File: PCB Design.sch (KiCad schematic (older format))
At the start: 14 parts

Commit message: Main schematic finished
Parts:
- added D? (x4): D_Small, symbol Device:D_Small
- added F?: 500mA, symbol Device:Polyfuse_Small
- added MX? (x4): MX-NoLED, symbol MX_Alps_Hybrid:MX-NoLED
- added USB?: Molex-0548190589, symbol random-keyboard-parts:Molex-0548190589
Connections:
- net labels added: VCC, col0, col1, row0, row1
- wire segments 46 -> 72
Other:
- moved on the sheet: C?, R?, SW?, U?, Y?

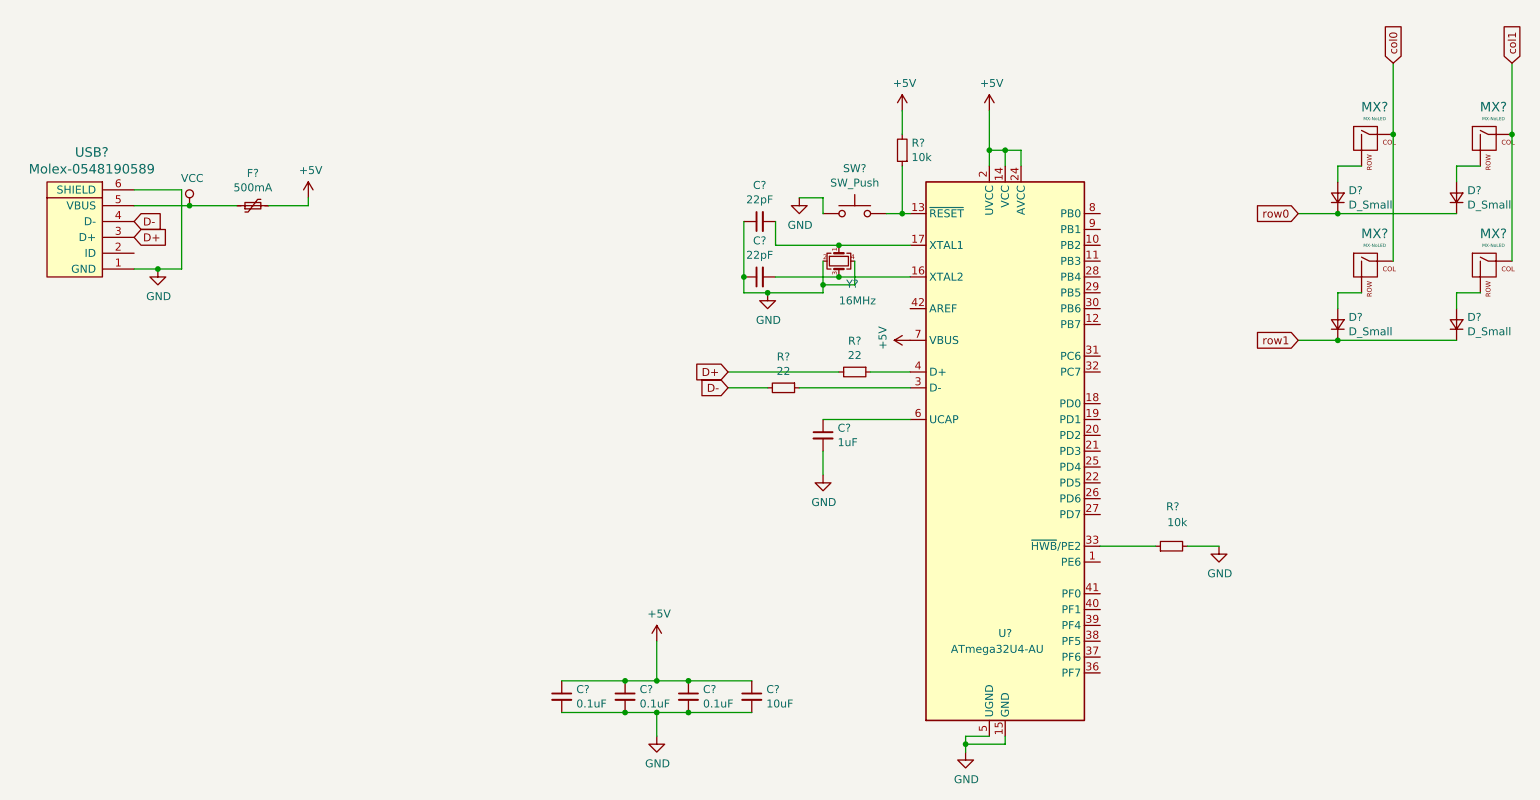
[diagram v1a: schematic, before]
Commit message: Assigning library components to schematic, need to figure out mx_alps_hybrid library issue
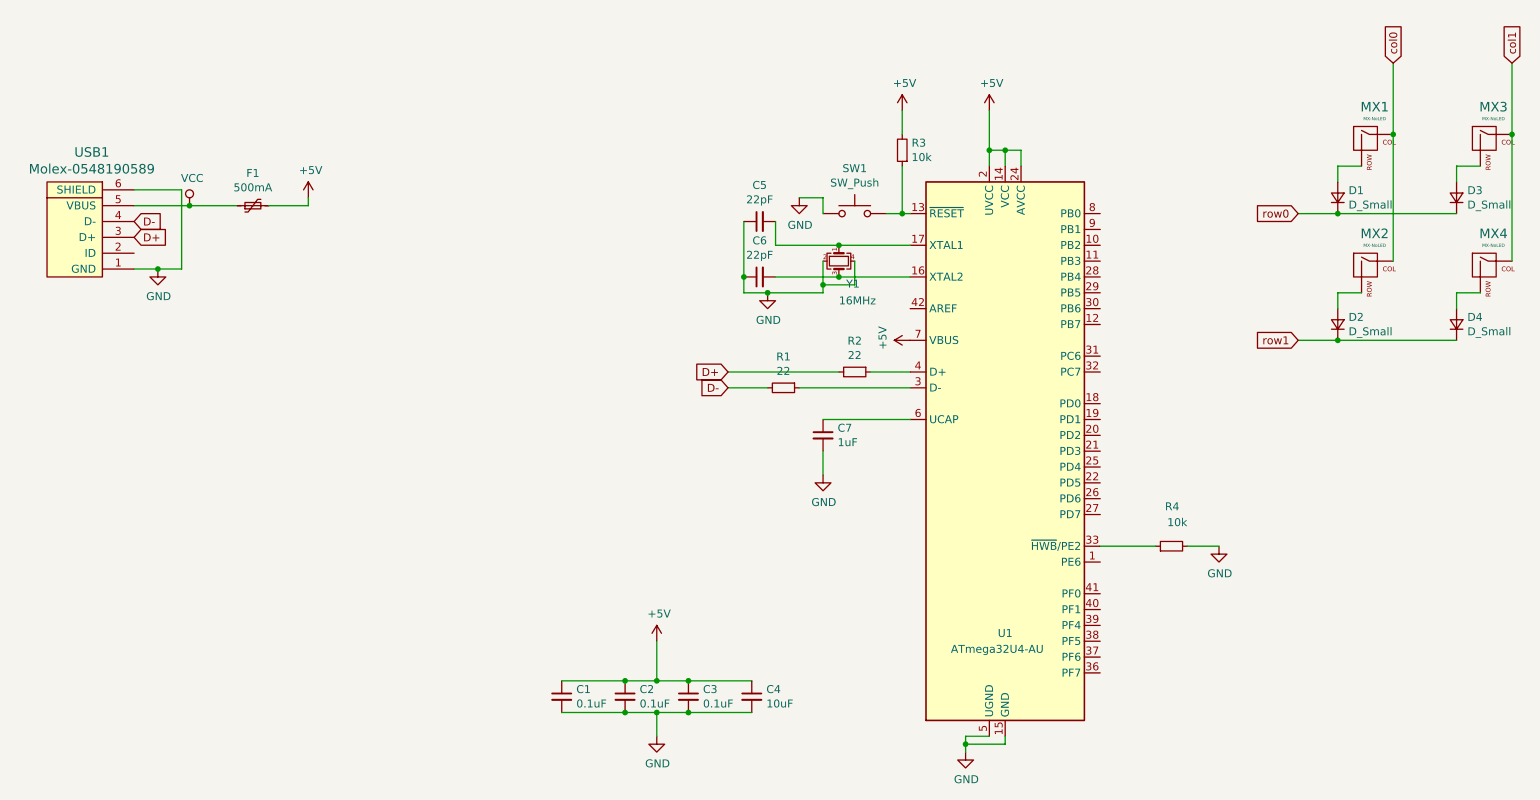
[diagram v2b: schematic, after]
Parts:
- C1, C2, C3, C4, C5, C6, C7: renamed from C?; footprint (none) -> Capacitor_SMD:C_0805_2012Metric
- D1, D2, D3, D4: renamed from D?; footprint (none) -> Diode_SMD:D_SOD-123
- F1: renamed from F?; footprint (none) -> Fuse:Fuse_1206_3216Metric
- R1, R2, R3, R4: renamed from R?; footprint (none) -> Resistor_SMD:R_0805_2012Metric
- SW1: renamed from SW?; footprint (none) -> random-keyboard-parts:SKQG-1155865
- USB1: renamed from USB?; footprint (none) -> random-keyboard-parts:Molex-0548190589
- Y1: renamed from Y?; footprint (none) -> Crystal:Crystal_SMD_3225-4Pin_3.2x2.5mm
- gave numbers to parts that had none: 5

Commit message: Figured out mx lib issue
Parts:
- MX1, MX2, MX3, MX4: footprint (none) -> MX_Alps_Hybrid1:MX-1U-NoLED
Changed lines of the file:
@@
 F 0 "MX1" H 10133 1523 60  0000 C CNN
 F 1 "MX-NoLED" H 10133 1449 20  0000 C CNN
-F 2 "" H 9475 1275 60  0001 C CNN
+F 2 "MX_Alps_Hybrid1:MX-1U-NoLED" H 9475 1275 60  0001 C CNN
 F 3 "" H 9475 1275 60  0001 C CNN
 	1    10100 1300
@@
 F 0 "MX3" H 10883 1523 60  0000 C CNN
 F 1 "MX-NoLED" H 10883 1449 20  0000 C CNN
-F 2 "" H 10225 1275 60  0001 C CNN
+F 2 "MX_Alps_Hybrid1:MX-1U-NoLED" H 10225 1275 60  0001 C CNN
 F 3 "" H 10225 1275 60  0001 C CNN
 	1    10850 1300
@@
 F 0 "MX2" H 10133 2323 60  0000 C CNN
 F 1 "MX-NoLED" H 10133 2249 20  0000 C CNN
-F 2 "" H 9475 2075 60  0001 C CNN
+F 2 "MX_Alps_Hybrid1:MX-1U-NoLED" H 9475 2075 60  0001 C CNN
 F 3 "" H 9475 2075 60  0001 C CNN
 	1    10100 2100
@@
 F 0 "MX4" H 10883 2323 60  0000 C CNN
 F 1 "MX-NoLED" H 10883 2249 20  0000 C CNN
-F 2 "" H 10225 2075 60  0001 C CNN
+F 2 "MX_Alps_Hybrid1:MX-1U-NoLED" H 10225 2075 60  0001 C CNN
 F 3 "" H 10225 2075 60  0001 C CNN
 	1    10850 2100

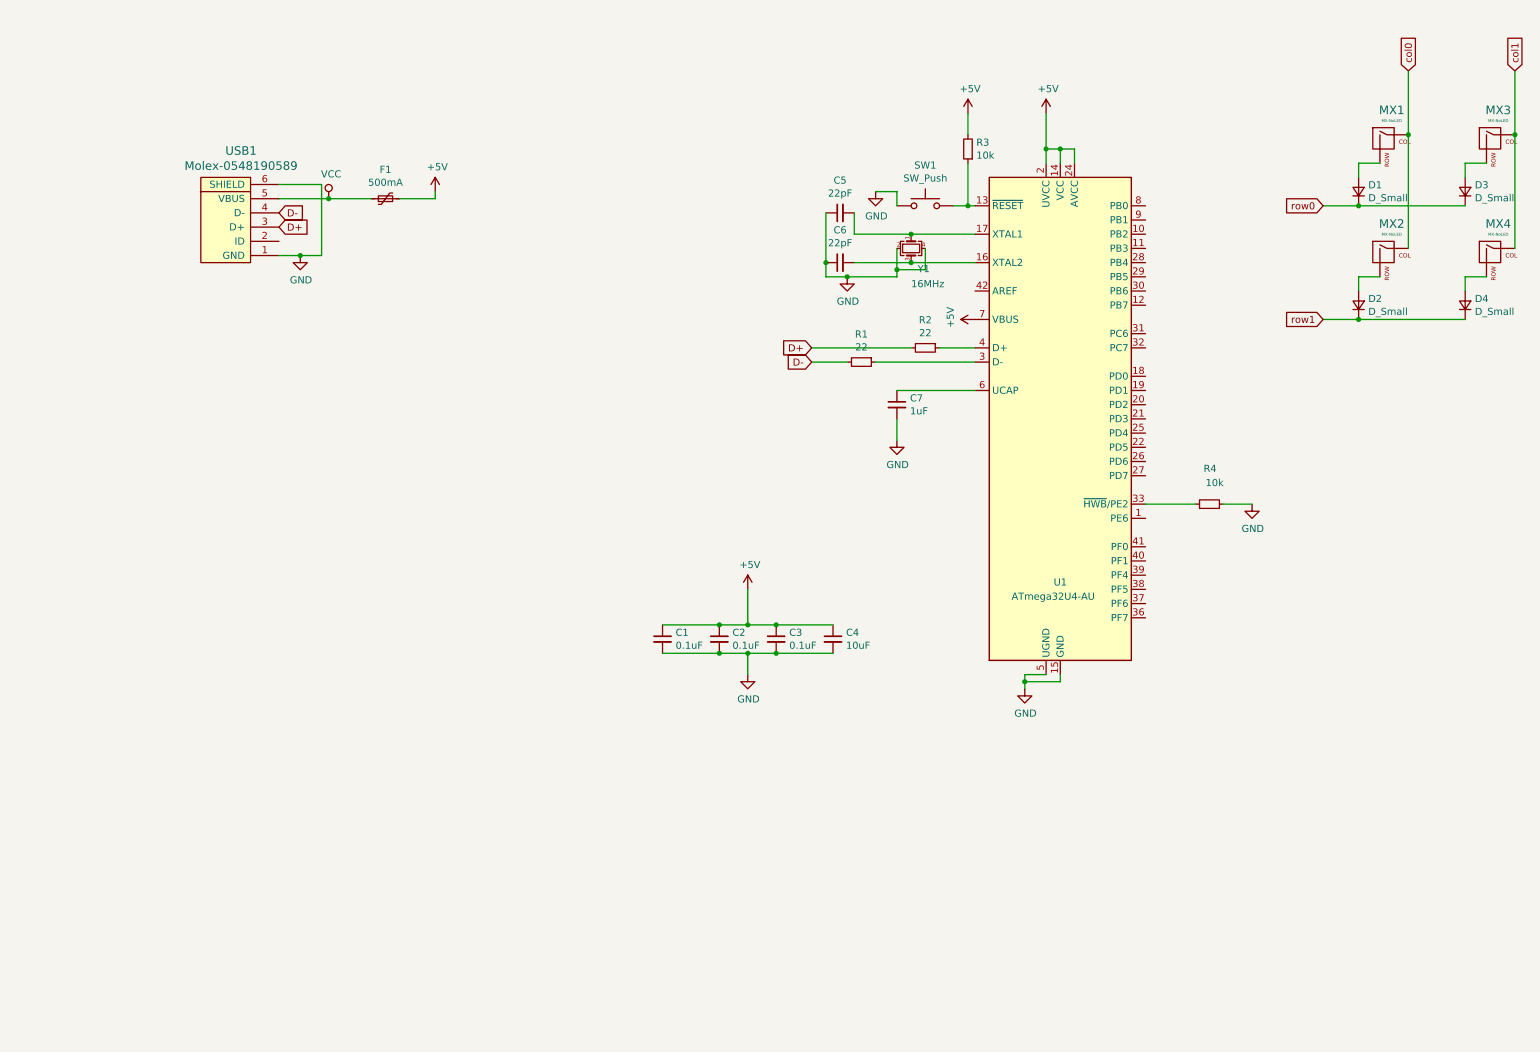
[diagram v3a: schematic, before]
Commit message: Diode layout completed
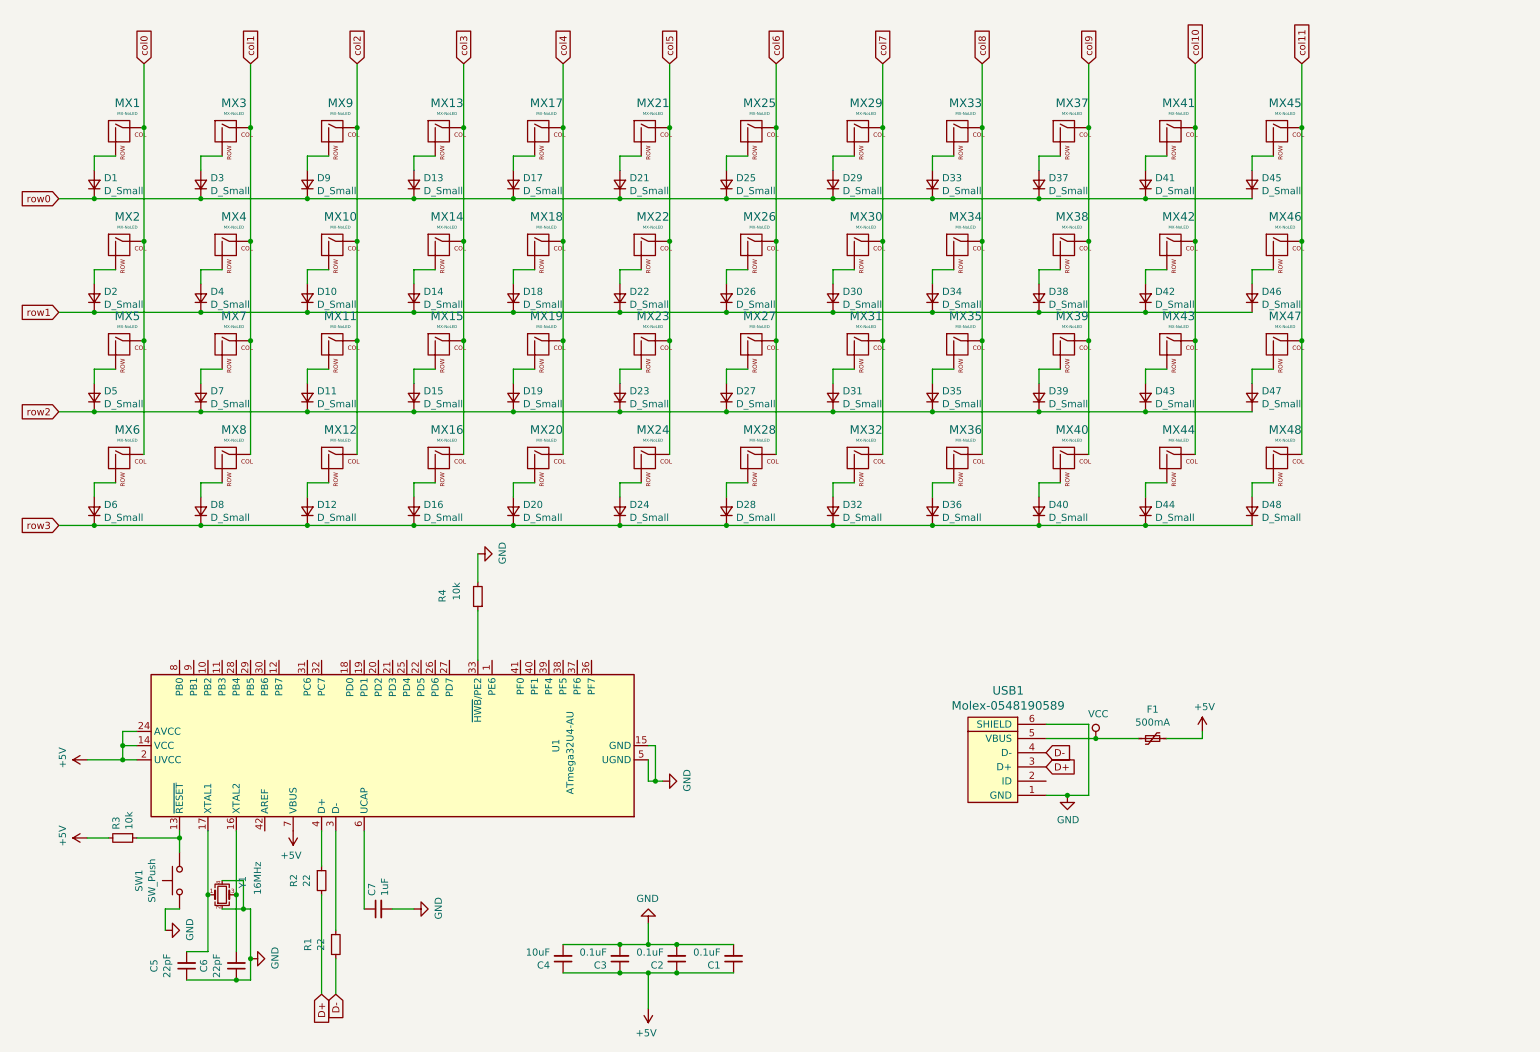
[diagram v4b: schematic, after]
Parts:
- added D10, D11, D12, D13, D14, D15, D16, D17, D18, D19, D20, D21, D22, D23, D24, D25, D26, D27, D28, D29, D30, D31, D32, D33, D34, D35, D36, D37, D38, D39, D40, D41, D42, D43, D44, D45, D46, D47, D48, D5, D6, D7, D8, D9: D_Small, Diode_SMD:D_SOD-123, symbol Device:D_Small
- added MX10, MX11, MX12, MX13, MX14, MX15, MX16, MX17, MX18, MX19, MX20, MX21, MX22, MX23, MX24, MX25, MX26, MX27, MX28, MX29, MX30, MX31, MX32, MX33, MX34, MX35, MX36, MX37, MX38, MX39, MX40, MX41, MX42, MX43, MX44, MX45, MX46, MX47, MX48, MX5, MX6, MX7, MX8, MX9: MX-NoLED, MX_Alps_Hybrid1:MX-1U-NoLED, symbol MX_Alps_Hybrid:MX-NoLED
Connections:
- net col0: now also MX5.1 (COL), MX6.1 (COL)
- net col1: now also MX7.1 (COL), MX8.1 (COL)
- net row0: now also D13.1 (K), D17.1 (K), D21.1 (K), D25.1 (K), D29.1 (K), D33.1 (K), D37.1 (K), D41.1 (K), D45.1 (K), D9.1 (K)
- net row1: now also D10.1 (K), D14.1 (K), D18.1 (K), D22.1 (K), D26.1 (K), D30.1 (K), D34.1 (K), D38.1 (K), D42.1 (K), D46.1 (K)
- new net: D9.2 (A), MX9.2 (ROW)
- new net: D13.2 (A), MX13.2 (ROW)
- new net: D10.2 (A), MX10.2 (ROW)
- new net: D14.2 (A), MX14.2 (ROW)
- new net: D5.2 (A), MX5.2 (ROW)
- new net: D7.2 (A), MX7.2 (ROW)
- new net: D6.2 (A), MX6.2 (ROW)
- new net: D8.2 (A), MX8.2 (ROW)
- new net: D16.2 (A), MX16.2 (ROW)
- new net: D12.2 (A), MX12.2 (ROW)
- new net: D15.2 (A), MX15.2 (ROW)
- new net: D11.2 (A), MX11.2 (ROW)
- new net: D17.2 (A), MX17.2 (ROW)
- new net: D21.2 (A), MX21.2 (ROW)
- new net: D18.2 (A), MX18.2 (ROW)
- new net: D22.2 (A), MX22.2 (ROW)
- new net: D30.2 (A), MX30.2 (ROW)
- new net: D26.2 (A), MX26.2 (ROW)
- new net: D29.2 (A), MX29.2 (ROW)
- new net: D25.2 (A), MX25.2 (ROW)
- new net: D19.2 (A), MX19.2 (ROW)
- new net: D23.2 (A), MX23.2 (ROW)
- new net: D20.2 (A), MX20.2 (ROW)
- new net: D24.2 (A), MX24.2 (ROW)
- new net: D32.2 (A), MX32.2 (ROW)
- new net: D28.2 (A), MX28.2 (ROW)
- new net: D31.2 (A), MX31.2 (ROW)
- new net: D27.2 (A), MX27.2 (ROW)
- new net: D33.2 (A), MX33.2 (ROW)
- new net: D37.2 (A), MX37.2 (ROW)
- new net: D34.2 (A), MX34.2 (ROW)
- new net: D38.2 (A), MX38.2 (ROW)
- new net: D46.2 (A), MX46.2 (ROW)
- new net: D42.2 (A), MX42.2 (ROW)
- new net: D45.2 (A), MX45.2 (ROW)
- new net: D41.2 (A), MX41.2 (ROW)
- new net: D35.2 (A), MX35.2 (ROW)
- new net: D39.2 (A), MX39.2 (ROW)
- new net: D36.2 (A), MX36.2 (ROW)
- new net: D40.2 (A), MX40.2 (ROW)
- new net: D48.2 (A), MX48.2 (ROW)
- new net: D44.2 (A), MX44.2 (ROW)
- new net: D47.2 (A), MX47.2 (ROW)
- new net: D43.2 (A), MX43.2 (ROW)
- new net col10: MX41.1 (COL), MX42.1 (COL), MX43.1 (COL), MX44.1 (COL)
- new net col11: MX45.1 (COL), MX46.1 (COL), MX47.1 (COL), MX48.1 (COL)
- new net col2: MX10.1 (COL), MX11.1 (COL), MX12.1 (COL), MX9.1 (COL)
- new net col3: MX13.1 (COL), MX14.1 (COL), MX15.1 (COL), MX16.1 (COL)
- new net col4: MX17.1 (COL), MX18.1 (COL), MX19.1 (COL), MX20.1 (COL)
- new net col5: MX21.1 (COL), MX22.1 (COL), MX23.1 (COL), MX24.1 (COL)
- new net col6: MX25.1 (COL), MX26.1 (COL), MX27.1 (COL), MX28.1 (COL)
- new net col7: MX29.1 (COL), MX30.1 (COL), MX31.1 (COL), MX32.1 (COL)
- new net col8: MX33.1 (COL), MX34.1 (COL), MX35.1 (COL), MX36.1 (COL)
- new net col9: MX37.1 (COL), MX38.1 (COL), MX39.1 (COL), MX40.1 (COL)
- new net row2: D11.1 (K), D15.1 (K), D19.1 (K), D23.1 (K), D27.1 (K), D31.1 (K), D35.1 (K), D39.1 (K), D43.1 (K), D47.1 (K), D5.1 (K), D7.1 (K)
- new net row3: D12.1 (K), D16.1 (K), D20.1 (K), D24.1 (K), D28.1 (K), D32.1 (K), D36.1 (K), D40.1 (K), D44.1 (K), D48.1 (K), D6.1 (K), D8.1 (K)
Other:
- moved on the sheet: C1, C2, C3, C4, C5, C6, C7, D1, D2, D3, D4, F1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

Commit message: Finished routing
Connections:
- net col0: now also U1.41 (PF0)
- net col1: now also U1.40 (PF1)
- net col10: now also U1.26 (PD6)
- net col11: now also U1.25 (PD4)
- net col2: now also U1.39 (PF4)
- net col3: now also U1.38 (PF5)
- net col4: now also U1.37 (PF6)
- net col5: now also U1.11 (PB3)
- net col6: now also U1.22 (PD5)
- net col7: now also U1.29 (PB5)
- net col8: now also U1.28 (PB4)
- net col9: now also U1.27 (PD7)
- net row0: now also U1.12 (PB7)
- net row1: now also U1.21 (PD3)
- net row2: now also U1.32 (PC7)
- net row3: now also U1.31 (PC6)
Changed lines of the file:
@@
 	6200 4000 6900 4000
 Connection ~ 6200 4000
+Text GLabel 3300 4950 1    50   Input ~ 0
+col6
+Text GLabel 3100 4950 1    50   Input ~ 0
+row1
+Text GLabel 2300 4950 1    50   Input ~ 0
+row0
+Text GLabel 1900 4950 1    50   Input ~ 0
+col5
+Text GLabel 3200 4950 1    50   Input ~ 0
+col11
+Text GLabel 3400 4950 1    50   Input ~ 0
+col10
+Text GLabel 3500 4950 1    50   Input ~ 0
+col9
+Text GLabel 2000 4950 1    50   Input ~ 0
+col8
+Text GLabel 2100 4950 1    50   Input ~ 0
+col7
+Text GLabel 2500 4950 1    50   Input ~ 0
+row3
+Text GLabel 2600 4950 1    50   Input ~ 0
+row2
+Text GLabel 4000 4950 1    50   Input ~ 0
+col0
+Text GLabel 4100 4950 1    50   Input ~ 0
+col1
+Text GLabel 4200 4950 1    50   Input ~ 0
+col2
+Text GLabel 4300 4950 1    50   Input ~ 0
+col3
+Text GLabel 4400 4950 1    50   Input ~ 0
+col4
 $EndSCHEMATC
